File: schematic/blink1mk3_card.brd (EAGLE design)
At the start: 14.9 x 9.6 mm, 15 parts, among them U1 EFM32HG309F64G, X2 USBPCB2

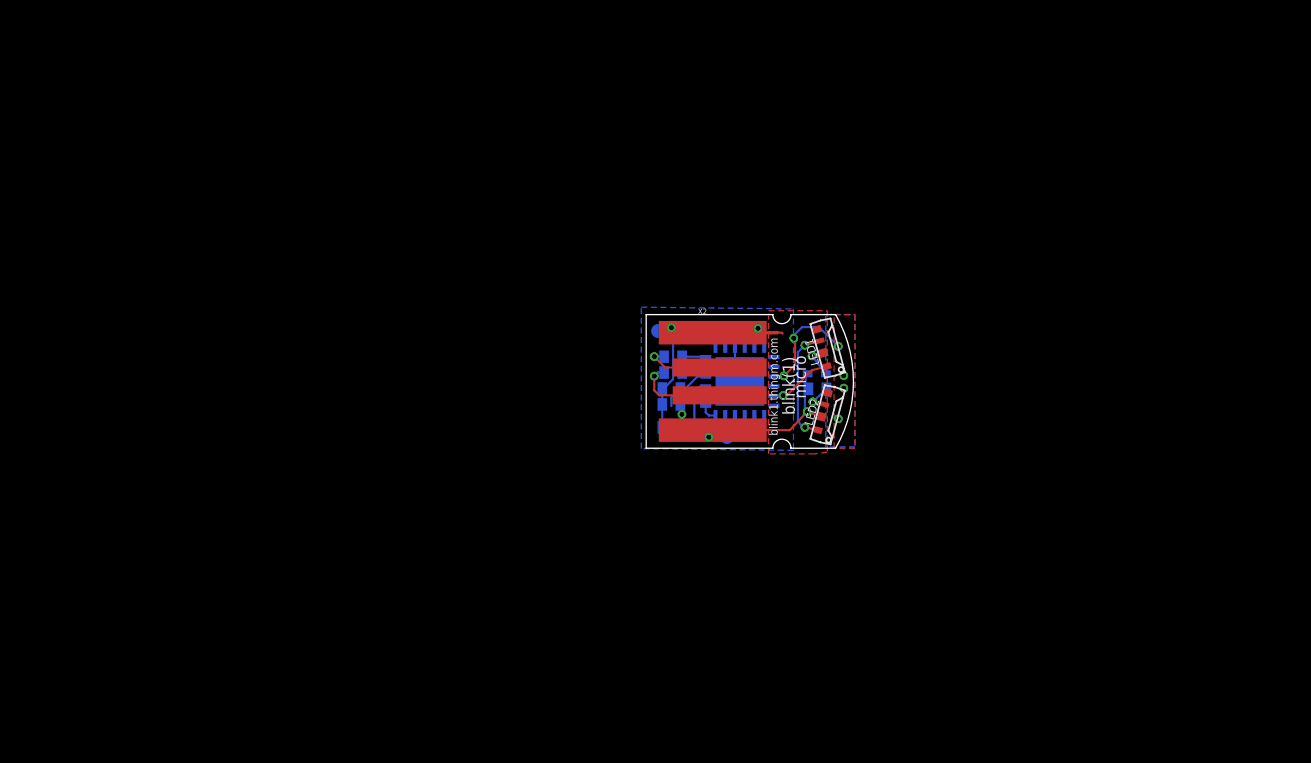
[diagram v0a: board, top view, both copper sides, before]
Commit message: added business card variant, and 3535 LED variant
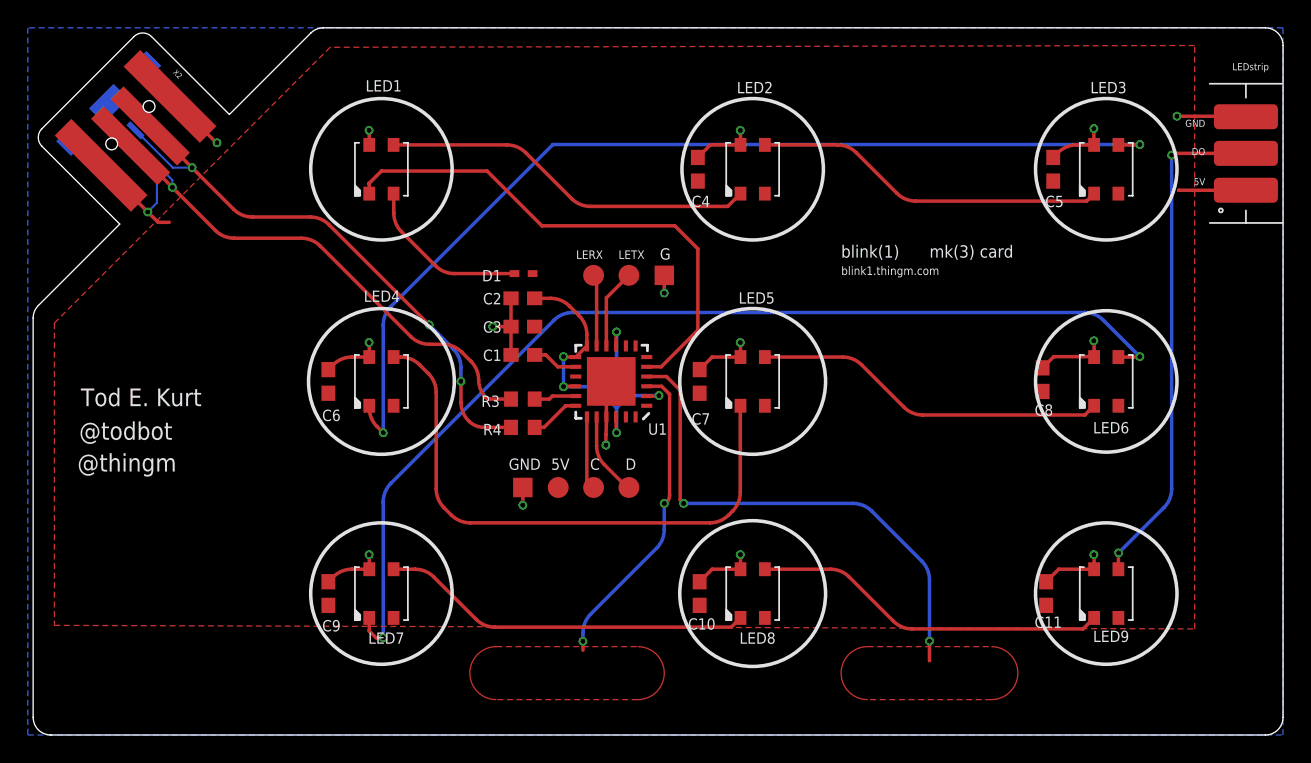
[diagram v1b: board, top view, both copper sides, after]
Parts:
- added C10, C11, C5, C6, C7, C8, C9: 0.1uF, adafruit:C0603
- added GND: TPTP14SQ, testpad:TP14SQ
- added J1: (no value), SparkFun-Connectors:USB-B-MICRO-SMD
- added LED3, LED4, LED5, LED6, LED7, LED8, LED9: WS2812B3535, adafruit:LED3535
- added LERX, LETX: TPTP15R, testpad:TP15R
- added U$1: LED_STRIP_3P, NeoJoints:LEDSTRIP-3P
- 5V, C, D: value TPTP10R -> TPTP15R; device testpad:TP10R -> testpad:TP15R
- C1, C2, C3, C4: device adafruit:C0402 -> adafruit:C0603
- G: value TPTP10R -> TPTP14SQ; device testpad:TP10R -> testpad:TP14SQ
- LED1, LED2: value WS2812B4020SIDE -> WS2812B3535; device todstuff:SK6812-SIDE -> adafruit:LED3535
- R3, R4: device adafruit:R0402 -> adafruit:R0603
- moved X2 45.2 mm to (-36.9, 17.0), turned to 315 degrees
- moved LED1 34.6 mm to (-20.3, 15.2), turned to 90 degrees
- moved D1 22.4 mm to (-10.2, 7.75), flipped to the top
- moved LED2 18.5 mm to (6.35, 15.2), turned to 90 degrees
- moved C4 18.0 mm to (2.41, 15.2), flipped to the top, turned to 90 degrees
- moved C 13.4 mm to (-5.08, -7.62), flipped to the top
- moved D 13.3 mm to (-2.54, -7.62), flipped to the top
- moved 5V 12.6 mm to (-7.62, -7.62), flipped to the top
- moved C2 12.5 mm to (-10.2, 5.97), flipped to the top, turned to 180 degrees
- moved C3 12.0 mm to (-10.2, 3.94), flipped to the top, turned to 180 degrees
- moved R4 11.9 mm to (-10.2, -3.30), flipped to the top, turned to 180 degrees
- moved C1 11.9 mm to (-10.2, 1.91), flipped to the top, turned to 180 degrees
- moved R3 11.0 mm to (-10.2, -1.27), flipped to the top, turned to 180 degrees
- moved U1 9.24 mm to (-3.81, 0.00), flipped to the top, turned to 180 degrees
- moved G 4.03 mm to (0.00, 7.62), flipped to the top
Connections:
- new net N$10: LED6.3, LED7.1
- new net N$4: LED7.3, LED8.1
- new net N$5: LED4.3, LED5.1
- new net N$6: LED5.3, LED6.1
- new net N$7: LED2.3, LED3.1
- new net N$8: LED3.3, LED4.1
- new net N$9: LED8.3, LED9.1
- net +5V: now also C10.1, C11.1, C5.1, C6.1, C7.1, C8.1, C9.1, J1.VBUS, LED2.2, LED3.2, LED4.2, LED5.2, LED6.2, LED7.2, LED8.2, LED9.2, U$1.A; no longer LED2.1-VDD
- net DI: now also LED1.1; no longer LED1.4-DIN
- net DO: now also LED9.3, U$1.B; no longer LED2.2-DOUT
- net GND: now also C10.2, C11.2, C5.2, C6.2, C7.2, C8.2, C9.2, GND.TP, J1.GND, LED1.4, LED2.4, LED3.4, LED4.4, LED5.4, LED6.4, LED7.4, LED8.4, LED9.4, U$1.C; no longer LED1.3-GND, LED2.3-GND
- net LEUO_RX: now also LERX.TP
- net LEUO_TX: now also LETX.TP
- net N$2: now also LED1.3, LED2.1; no longer LED1.2-DOUT, LED2.4-DIN
- net USB_D+: now also J1.D+
- net USB_D-: now also J1.D-
- net VLEDA: now also LED1.2; no longer LED1.1-VDD
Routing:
- net N$10: track 0.00 -> 74.9 mm, vias 0 -> 2
- net N$8: track 0.00 -> 71.7 mm, vias 0 -> 2
- net N$5: track 0.00 -> 41.7 mm
- net CAP1A: track 0.00 -> 37.0 mm, vias 0 -> 2
- net DO: track 0.00 -> 36.6 mm, vias 0 -> 2
- net USB_D+: track 5.73 -> 41.9 mm, vias 1 -> 3
- net USB_D-: track 6.68 -> 39.9 mm
- net DI: track 4.68 -> 37.7 mm, vias 1 -> 0
- net GND: track 27.2 -> 59.5 mm, vias 3 -> 15
- net N$4: track 0.00 -> 26.7 mm
- net N$9: track 0.00 -> 25.5 mm
- net N$6: track 0.00 -> 25.4 mm
- net N$7: track 0.00 -> 25.3 mm
- net +3V3: track 6.94 -> 28.9 mm, vias 0 -> 5
- net N$2: track 8.42 -> 26.9 mm, vias 2 -> 0
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- added copper zone on layer 1, net +5V
- added copper zone on layer 1, net CAP1A
- added copper zone on layer 16, net GND
- removed copper zone on layer 16, net +3V3
- removed copper zone on layer 16, net CAP0A
- removed copper zone on layer 1, net GND
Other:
- board size 14.9 x 9.6 mm -> 89.8 x 50.8 mm
- board text added: "5V"
- board text added: "@thingm"
- board text added: "@todbot"
- board text added: "DO"
- board text added: "GND"
- board text added: "Gnd"
- board text added: "LEDstrip"
- board text added: "Tod E. Kurt"
- board text added: "blink1mk3_002"
- board text added: "mk(3) card"
- board text removed: "blink1mk3micro1"
- board text removed: "micro"

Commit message: card layout update
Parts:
- moved C8 0.77 mm to (27.9, 0.00)
- moved C11 0.51 mm to (27.9, -15.2)
- moved C4 0.13 mm to (2.54, 15.2)
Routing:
- net +5V: track 17.7 -> 30.9 mm
- net GND: track 59.5 -> 58.7 mm
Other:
- board text added: "A"
- board text added: "B"
